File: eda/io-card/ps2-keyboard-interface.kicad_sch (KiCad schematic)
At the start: 11 parts, among them J1 PS2, U3 74HCT14, U6 74HCT595, U7 74HCT595

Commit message: Add expansion backplane
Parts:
- J1: footprint (none) -> Local:Connector_Mini-DIN_Female_6Pin_2rows
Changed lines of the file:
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@@
     (stroke (width 0) (type default))
   )
-  (label "KeyboardBit6" (at 186.69 54.61 0)
-    (effects (font (size 1.27 1.27)) (justify left bottom))
-  )
-  (label "KeyboardBit2" (at 186.69 44.45 0)
+  (label "KeyboardBit6" (at 186.69 54.61 0) (fields_autoplaced)
+    (effects (font (size 1.27 1.27)) (justify left bottom))
+  )
+  (label "KeyboardBit2" (at 186.69 44.45 0) (fields_autoplaced)
     (effects (font (size 1.27 1.27)) (justify left bottom))
   )
@@
     (effects (font (size 1.27 1.27)) (justify right bottom))
   )
-  (label "KeyboardBit7" (at 187.325 92.075 0)
+  (label "KeyboardBit7" (at 187.325 92.075 0) (fields_autoplaced)
     (effects (font (size 1.27 1.27)) (justify left bottom))
   )
@@
     (effects (font (size 1.27 1.27)) (justify left bottom))
   )
-  (label "KeyboardBit0" (at 186.69 39.37 0)
+  (label "KeyboardBit0" (at 186.69 39.37 0) (fields_autoplaced)
     (effects (font (size 1.27 1.27)) (justify left bottom))
   )
@@
     (effects (font (size 1.27 1.27)) (justify right bottom))
   )
-  (label "KeyboardBit4" (at 186.69 49.53 0)
+  (label "KeyboardBit4" (at 186.69 49.53 0) (fields_autoplaced)
     (effects (font (size 1.27 1.27)) (justify left bottom))
   )
@@
     (effects (font (size 1.27 1.27)) (justify left bottom))
   )
-  (label "KeyboardBit1" (at 186.69 41.91 0)
+  (label "KeyboardBit1" (at 186.69 41.91 0) (fields_autoplaced)
     (effects (font (size 1.27 1.27)) (justify left bottom))
   )
@@
     (effects (font (size 1.27 1.27)) (justify left bottom))
   )
-  (label "KeyboardBit5" (at 186.69 52.07 0)
-    (effects (font (size 1.27 1.27)) (justify left bottom))
-  )
-  (label "KeyboardBit3" (at 186.69 46.99 0)
+  (label "KeyboardBit5" (at 186.69 52.07 0) (fields_autoplaced)
+    (effects (font (size 1.27 1.27)) (justify left bottom))
+  )
+  (label "KeyboardBit3" (at 186.69 46.99 0) (fields_autoplaced)
     (effects (font (size 1.27 1.27)) (justify left bottom))
   )
@@
       (effects (font (size 1.27 1.27)))
     )
-    (property "Footprint" "" (at 36.83 53.975 0)
-      (effects (font (size 1.27 1.27)) hide)
-    )
+    (property "Footprint" "Local:Connector_Mini-DIN_Female_6Pin_2rows" (at 36.83 53.975 0)
+      (effects (font (size 1.27 1.27)) hide)
+    )

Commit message: Normalize cap size
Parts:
- C1, C3, C4: footprint Capacitor_THT:C_Disc_D3.4mm_W2.1mm_P2.50mm -> Capacitor_THT:C_Disc_D3.8mm_W2.6mm_P2.50mm
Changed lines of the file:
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@@
       (effects (font (size 1.27 1.27)) (justify left))
     )
-    (property "Footprint" "Capacitor_THT:C_Disc_D3.4mm_W2.1mm_P2.50mm" (at 55.5752 102.87 0)
+    (property "Footprint" "Capacitor_THT:C_Disc_D3.8mm_W2.6mm_P2.50mm" (at 55.5752 102.87 0)
       (effects (font (size 1.27 1.27)) hide)
     )
@@
       (effects (font (size 1.27 1.27)) (justify left))
     )
-    (property "Footprint" "Capacitor_THT:C_Disc_D3.4mm_W2.1mm_P2.50mm" (at 42.8752 102.87 0)
+    (property "Footprint" "Capacitor_THT:C_Disc_D3.8mm_W2.6mm_P2.50mm" (at 42.8752 102.87 0)
       (effects (font (size 1.27 1.27)) hide)
     )
@@
       (effects (font (size 1.27 1.27)) (justify left))
     )
-    (property "Footprint" "Capacitor_THT:C_Disc_D3.4mm_W2.1mm_P2.50mm" (at 106.3752 45.085 0)
-      (effects (font (size 1.27 1.27)) hide)
-    )
+    (property "Footprint" "Capacitor_THT:C_Disc_D3.8mm_W2.6mm_P2.50mm" (at 106.3752 45.085 0)
+      (effects (font (size 1.27 1.27)) hide)
+    )

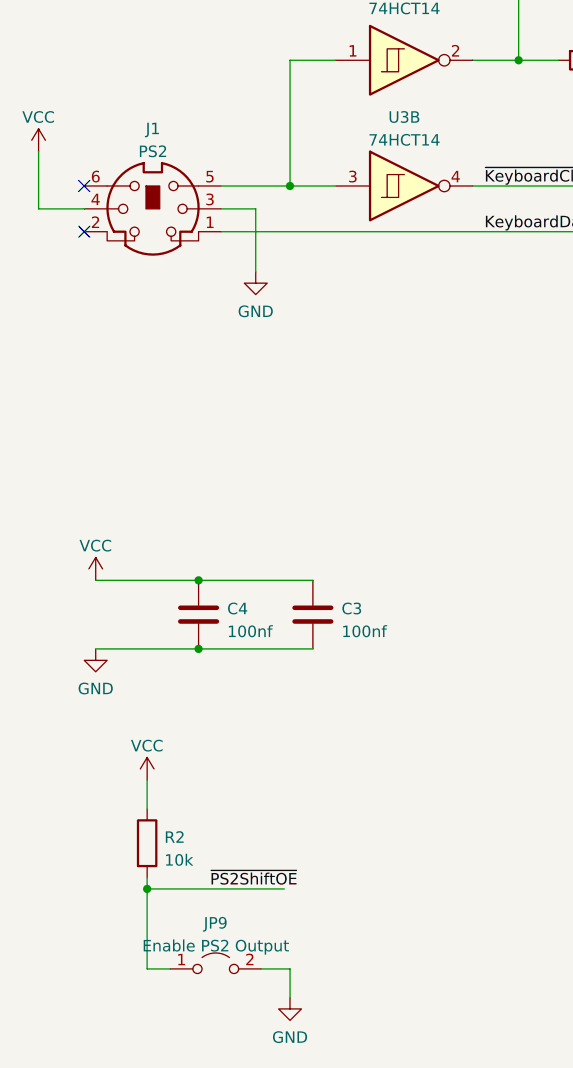
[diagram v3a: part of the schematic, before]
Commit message: Add SPI
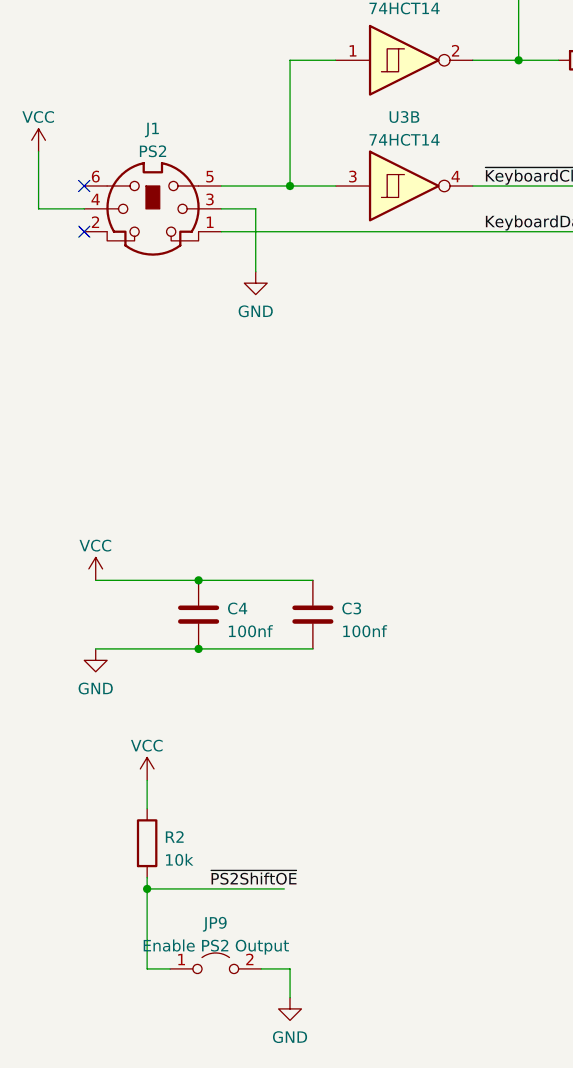
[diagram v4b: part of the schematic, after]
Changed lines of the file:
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@@
 (kicad_sch
-	(version 20231120)
+	(version 20250114)
 	(generator "eeschema")
-	(generator_version "8.0")
+	(generator_version "9.0")
 	(paper "A4")
 	(junction
@@
 	(label "KeyboardBit6"
 		(at 186.69 54.61 0)
-		(fields_autoplaced yes)
 		(effects
 			(font
@@
 	(label "KeyboardBit2"
 		(at 186.69 44.45 0)
-		(fields_autoplaced yes)
 		(effects
 			(font
@@
 	(label "~{PS2ShiftOE}"
 		(at 43.18 129.54 0)
-		(fields_autoplaced yes)
 		(effects
 			(font
@@
 	(label "~{PS2ShiftOE}"
 		(at 160.655 107.315 180)
-		(fields_autoplaced yes)
 		(effects
 			(font
@@
 	(label "KeyboardBit7"
 		(at 187.325 92.075 0)
-		(fields_autoplaced yes)
 		(effects
 			(font
@@
 	(label "~{KeyboardClk}"
 		(at 149.86 97.155 0)
-		(fields_autoplaced yes)
 		(effects
 			(font
@@
 	(label "KeyboardBit0"
 		(at 186.69 39.37 0)
-		(fields_autoplaced yes)
 		(effects
 			(font
@@
 	(label "KeyboardData"
 		(at 149.225 36.83 0)
-		(fields_autoplaced yes)
 		(effects
 			(font
@@
 	(label "~{KeyboardClk}"
 		(at 149.225 41.91 0)
-		(fields_autoplaced yes)
 		(effects
 			(font
@@
 	(label "~{PS2ShiftOE}"
 		(at 160.02 52.07 180)
-		(fields_autoplaced yes)
 		(effects
 			(font
@@
 	(label "KeyboardBit4"
 		(at 186.69 49.53 0)
-		(fields_autoplaced yes)
 		(effects
 			(font
@@
 	(label "~{KeyboardClk}"
 		(at 73.66 51.435 0)
-		(fields_autoplaced yes)
 		(effects
 			(font
@@
 	(label "KeyboardBit1"
 		(at 186.69 41.91 0)
-		(fields_autoplaced yes)
 		(effects
 			(font
@@
 	(label "KeyboardData"
 		(at 73.66 56.515 0)
-		(fields_autoplaced yes)
 		(effects
 			(font
@@
 	(label "KeyboardBit5"
 		(at 186.69 52.07 0)
-		(fields_autoplaced yes)
 		(effects
 			(font
@@
 	(label "KeyboardBit3"
 		(at 186.69 46.99 0)
-		(fields_autoplaced yes)
 		(effects
 			(font
@@
 		(shape output)
 		(at 116.84 64.135 0)
-		(fields_autoplaced yes)
 		(effects
 			(font
@@
 		(shape output)
 		(at 161.29 102.87 180)
-		(fields_autoplaced yes)
 		(effects
 			(font
@@
 		(shape output)
 		(at 229.87 28.575 0)
-		(fields_autoplaced yes)
 		(effects
 			(font
@@
 		(shape output)
 		(at 161.29 47.625 180)
-		(fields_autoplaced yes)
-		(effects
-			(font
+		(effects
+			(font
